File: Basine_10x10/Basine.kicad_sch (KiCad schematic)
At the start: 56 parts, among them J1 2060-451/998-404, J10 2060-451/998-404, J11 2060-451/998-404, J12 2060-451/998-404, J13 2060-451/998-404, J14 2060-451/998-404, J15 2060-451/998-404, J16 2060-451/998-404, J17 2060-451/998-404, J18 2060-451/998-404, J2 2060-451/998-404, J3 2060-451/998-404, J4 2060-451/998-404, J5 2060-451/998-404, J6 2060-451/998-404, J7 2060-451/998-404, J8 2060-451/998-404, J9 2060-451/998-404

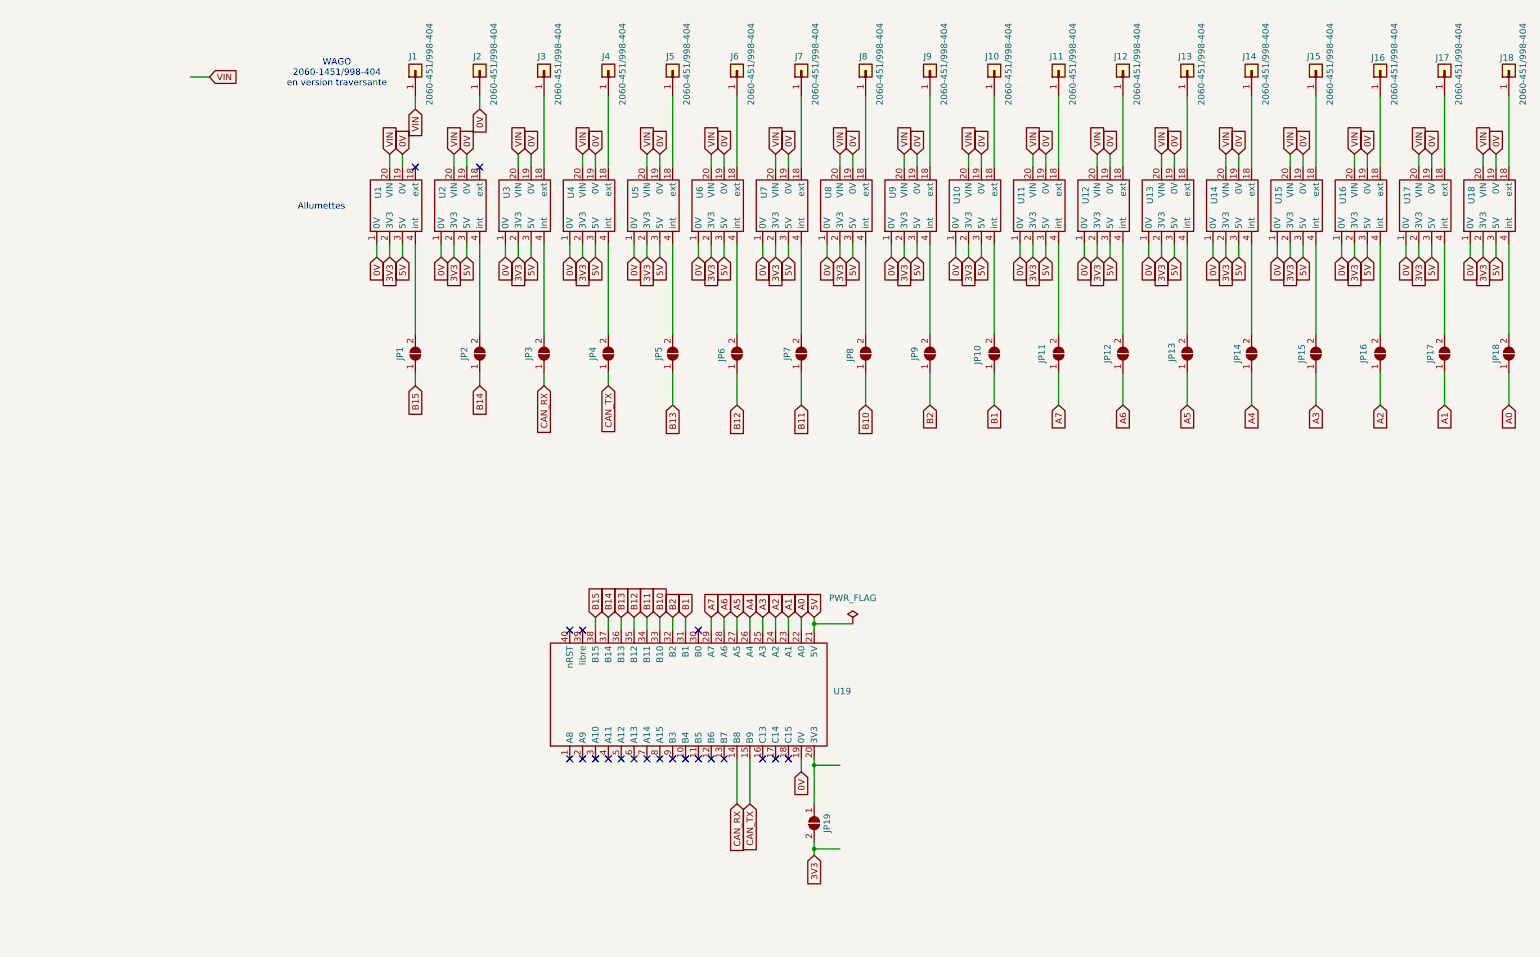
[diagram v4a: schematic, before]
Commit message: Basine_10x10 : recentrage ultro et ajout zone proto
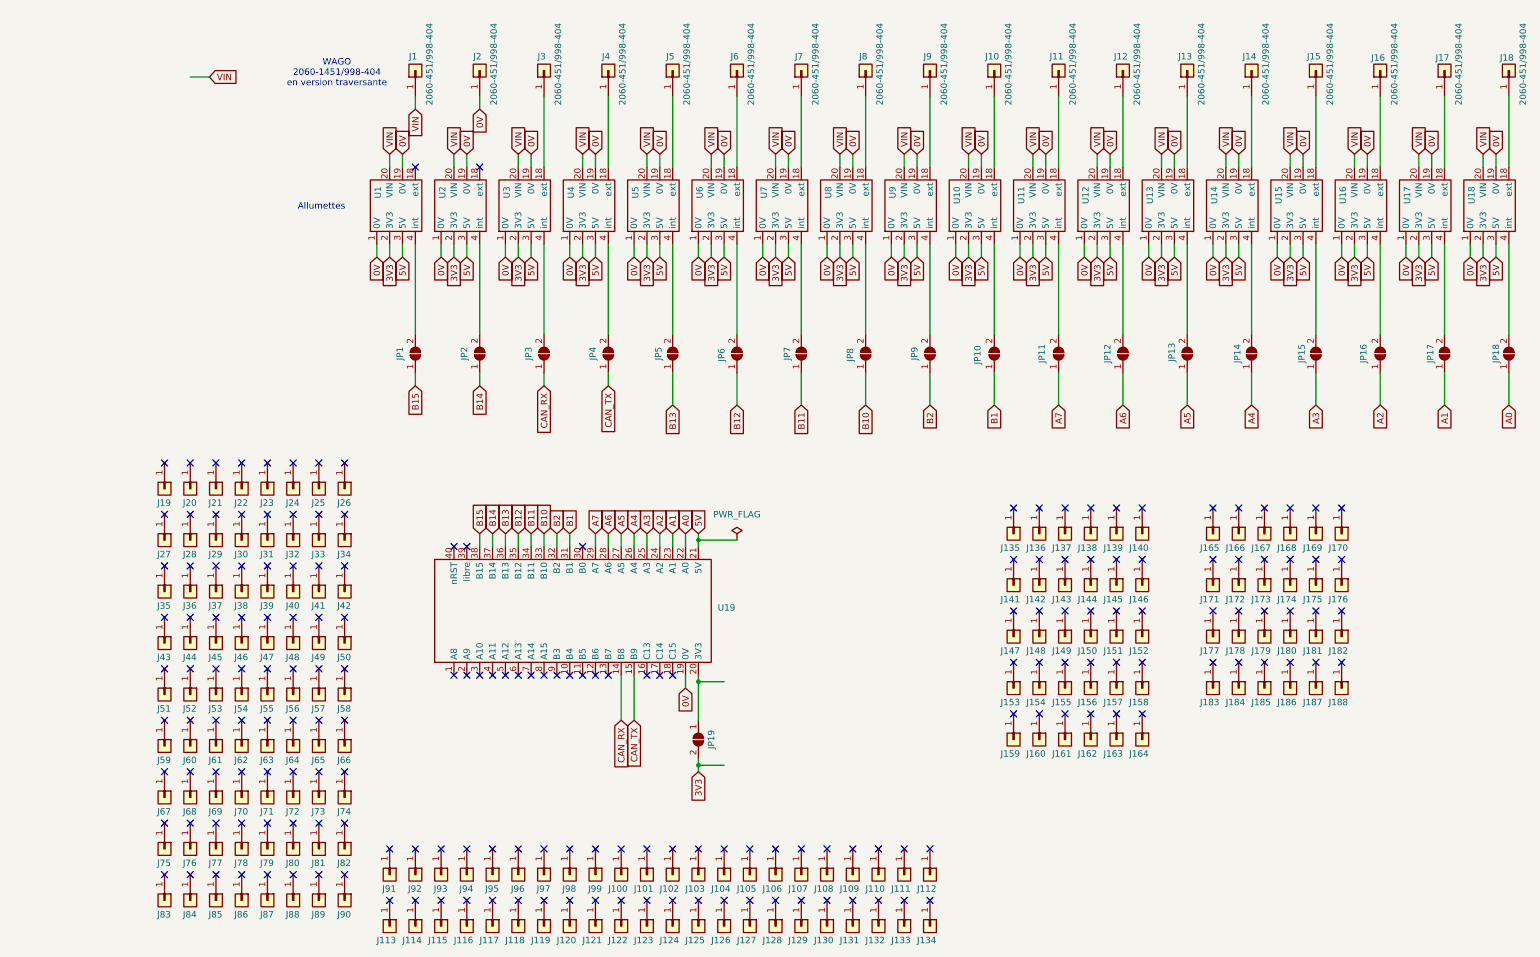
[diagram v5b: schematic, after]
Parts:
- added J100, J101, J102, J103, J104, J105, J106, J107, J108, J109, J110, J111, J112, J113, J114, J115, J116, J117, J118, J119, J120, J121, J122, J123, J124, J125, J126, J127, J128, J129, J130, J131, J132, J133, J134, J135, J136, J137, J138, J139, J140, J141, J142, J143, J144, J145, J146, J147, J148, J149, J150, J151, J152, J153, J154, J155, J156, J157, J158, J159, J160, J161, J162, J163, J164, J165, J166, J167, J168, J169, J170, J171, J172, J173, J174, J175, J176, J177, J178, J179, J180, J181, J182, J183, J184, J185, J186, J187, J188, J19, J20, J21, J22, J23, J24, J25, J26, J27, J28, J29, J30, J31, J32, J33, J34, J35, J36, J37, J38, J39, J40, J41, J42, J43, J44, J45, J46, J47, J48, J49, J50, J51, J52, J53, J54, J55, J56, J57, J58, J59, J60, J61, J62, J63, J64, J65, J66, J67, J68, J69, J70, J71, J72, J73, J74, J75, J76, J77, J78, J79, J80, J81, J82, J83, J84, J85, J86, J87, J88, J89, J90, J91, J92, J93, J94, J95, J96, J97, J98, J99: Pastille, Chimere_comps:Pastille_carree, symbol Connector_Generic:Conn_01x01
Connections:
- no-connect marks 21 -> 191
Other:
- moved on the sheet: JP19, U19
